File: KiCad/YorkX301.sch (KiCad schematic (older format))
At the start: 31 parts

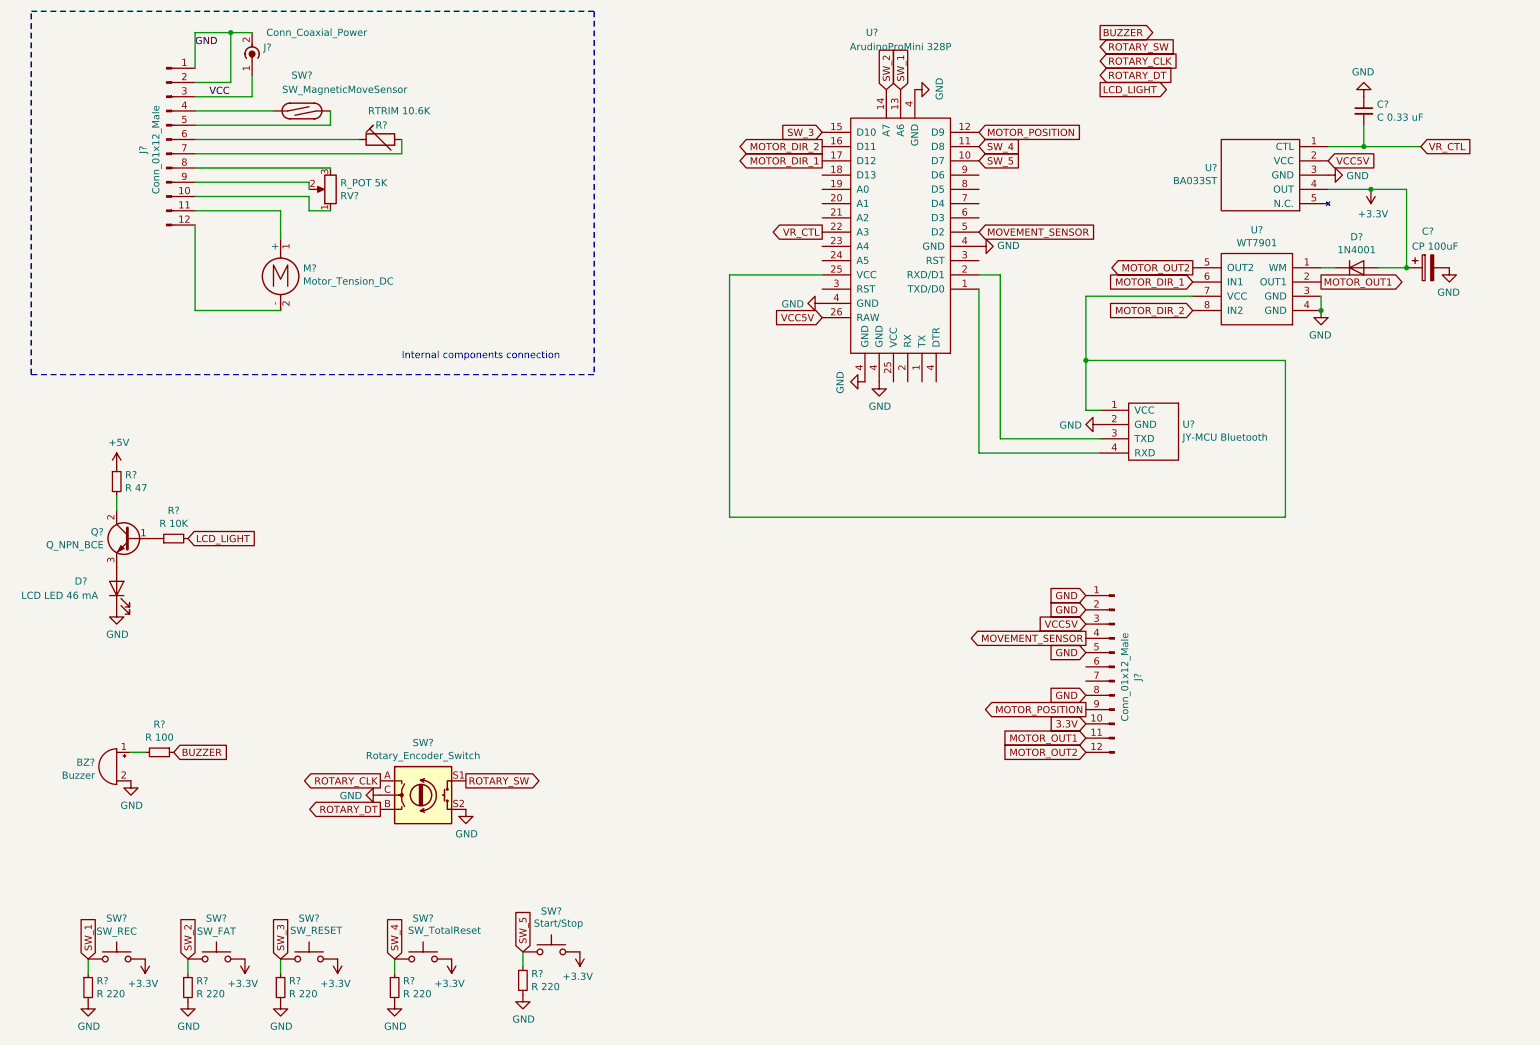
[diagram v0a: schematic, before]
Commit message: replaced WT7901 with DRV8833 rev 1.1
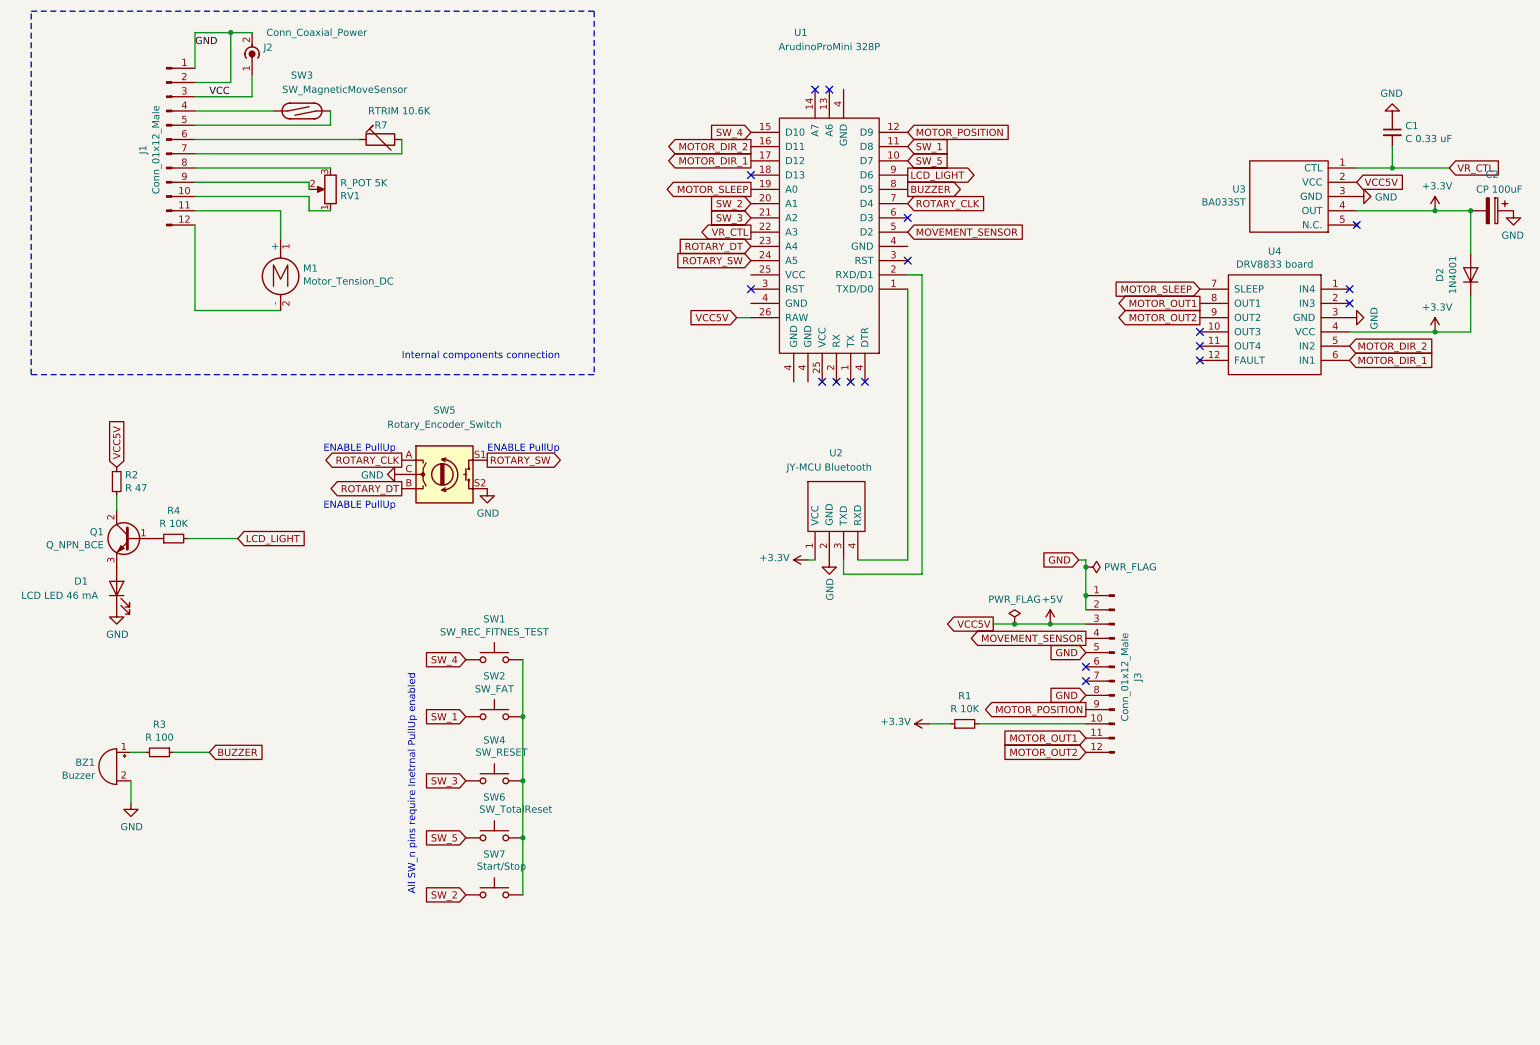
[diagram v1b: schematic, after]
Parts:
- removed R? (x5): R 220, symbol Device:R_Small
- removed U?: WT7901, symbol WT7901:WT7901
- added R1: R 10K, symbol Device:R_Small
- added U4: DRV8833 board, symbol DRV8833:DRV8833
- SW1: renamed from SW?; value SW_REC -> SW_REC_FITNES_TEST
- gave numbers to parts that had none: 24
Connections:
- net VCC5V is gone; now on net +5V: J3.3 (Pin_3), U1.26 (RAW), U3.2 (VCC)
- net +3V3: now also C2.2, D2.1 (K), U2.1 (VCC), R1.1, U4.4 (VCC); no longer C2.1, SW1.2, SW2.2, SW4.2, SW6.2, SW7.2
- net BUZZER: now also U1.8 (D5)
- net GND: now also C2.1, U4.3 (GND); no longer C2.2, U1.4 (GND)
- net LCD_LIGHT: now also U1.9 (D6)
- net MOTOR_DIR_1: now also U4.6 (IN1)
- net MOTOR_DIR_2: now also U4.5 (IN2)
- net MOTOR_OUT1: now also U4.8 (OUT1)
- net MOTOR_OUT2: now also U4.9 (OUT2)
- net ROTARY_CLK: now also U1.7 (D4)
- net ROTARY_DT: now also U1.23 (A4)
- net ROTARY_SW: now also U1.24 (A5)
- net SW_1: now also SW2.1, U1.11 (D8); no longer SW1.1, U1.13 (A6)
- net SW_2: now also SW7.1, U1.20 (A1); no longer SW2.1, U1.14 (A7)
- net SW_3: now also U1.21 (A2); no longer U1.15 (D10)
- net SW_4: now also SW1.1, U1.15 (D10); no longer SW6.1, U1.11 (D8)
- net SW_5: now also SW6.1; no longer SW7.1
- net at U1.25 (VCC): no longer U2.1 (VCC)
- net at U1.1 (TXD/D0): now also U2.4 (RXD)
- net MOTOR_SLEEP: now reaches U1.19 (A0)
- net MOTOR_SLEEP: now also U4.7 (SLEEP)
- net at U1.2 (RXD/D1): now also U2.3 (TXD)
- net 3.3V: no longer names the net of J3.10 (Pin_10)
- net 3.3V: now also R1.2
- new net: SW1.2, SW2.2, SW4.2, SW6.2, SW7.2
- no-connect marks 0 -> 18
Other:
- note added: "All SW_n pins require Inetrnal PullUp enabled"
- note added: "ENABLE PullUp"
- moved on the sheet: C1, C2, D2, SW1, SW2, SW4, SW5, SW6, SW7, U1, U2, U3
